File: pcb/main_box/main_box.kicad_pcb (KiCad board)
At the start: 2 copper layers, 150 x 70 mm, 20 parts, among them J1 AudioJack4, J13 Conn_01x06, J2 AudioJack4, J3 AudioJack4, J4 AudioJack4, J5 AudioJack4, J6 AudioJack4, J7 AudioJack4, J8 AudioJack4, SW1 SW_Push, SW2 SW_Push, SW3 SW_Push, SW4 SW_Push, SW5 SW_Push, SW6 SW_Push, U1 Pico

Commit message: Mby somewhat done...
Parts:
- removed J13: Conn_01x06, Connector_JST:JST_XH_B6B-XH-A_1x06_P2.50mm_Vertical
- added J9: Conn_01x06_MountingPin, Audio-jacks Libraries:JST_XH_S6B_combined_1x06, F.Cu at (145.1, 83.8)
- SW1, SW2, SW3, SW4, SW5, SW6: footprint Button_Switch_THT:SW_PUSH_6mm -> Audio-jacks Libraries:SW_PUSH_combined_6mm
- moved H1 16.0 mm to (53.5, 69.5)
- moved H2 16.0 mm to (196.5, 69.5)
- moved J4 5.00 mm to (191.5, 55.2)
- moved J5 5.00 mm to (58.5, 55.2)
- moved J3 4.00 mm to (177.0, 55.2)
- moved J6 4.00 mm to (73.0, 55.2)
- moved J2 3.00 mm to (162.5, 55.2)
- moved J7 3.00 mm to (87.5, 55.2)
- moved SW5 3.00 mm to (140.2, 113.2)
- moved SW6 3.00 mm to (116.2, 113.2)
- moved SW3 2.80 mm to (187.2, 92.0)
- moved SW4 2.80 mm to (178.5, 107.2)
- moved J1 2.00 mm to (148.0, 55.2)
- moved J8 2.00 mm to (102.0, 55.2)
- moved SW1 1.25 mm to (163.2, 98.5)
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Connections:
- J7 pad R2: /GPIO5 -> /GPIO3
- J7 pad T: /GPIO3 -> /GPIO5
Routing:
- net /GPIO5: track 24.4 -> 56.9 mm
- net /GPIO21: track 40.9 -> 64.1 mm
- net /GPIO20: track 56.7 -> 71.8 mm
- net /GPIO19: track 42.3 -> 56.4 mm
- net /GPIO12: track 152.5 -> 165.9 mm
- net /GPIO3: track 40.5 -> 30.5 mm
- net /GPIO13: track 149.2 -> 157.6 mm
- net /GPIO15: track 119.4 -> 127.7 mm
- net /GPIO18: track 51.6 -> 59.8 mm
- net /GPIO16: track 80.4 -> 86.6 mm
- net /GPIO9: track 56.0 -> 62.1 mm
- net /GPIO4: track 43.5 -> 37.4 mm
- net /GPIO17: track 85.5 -> 79.8 mm
- net /GPIO6: track 39.1 -> 44.5 mm
- net /GPIO14: track 140.3 -> 145.1 mm
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
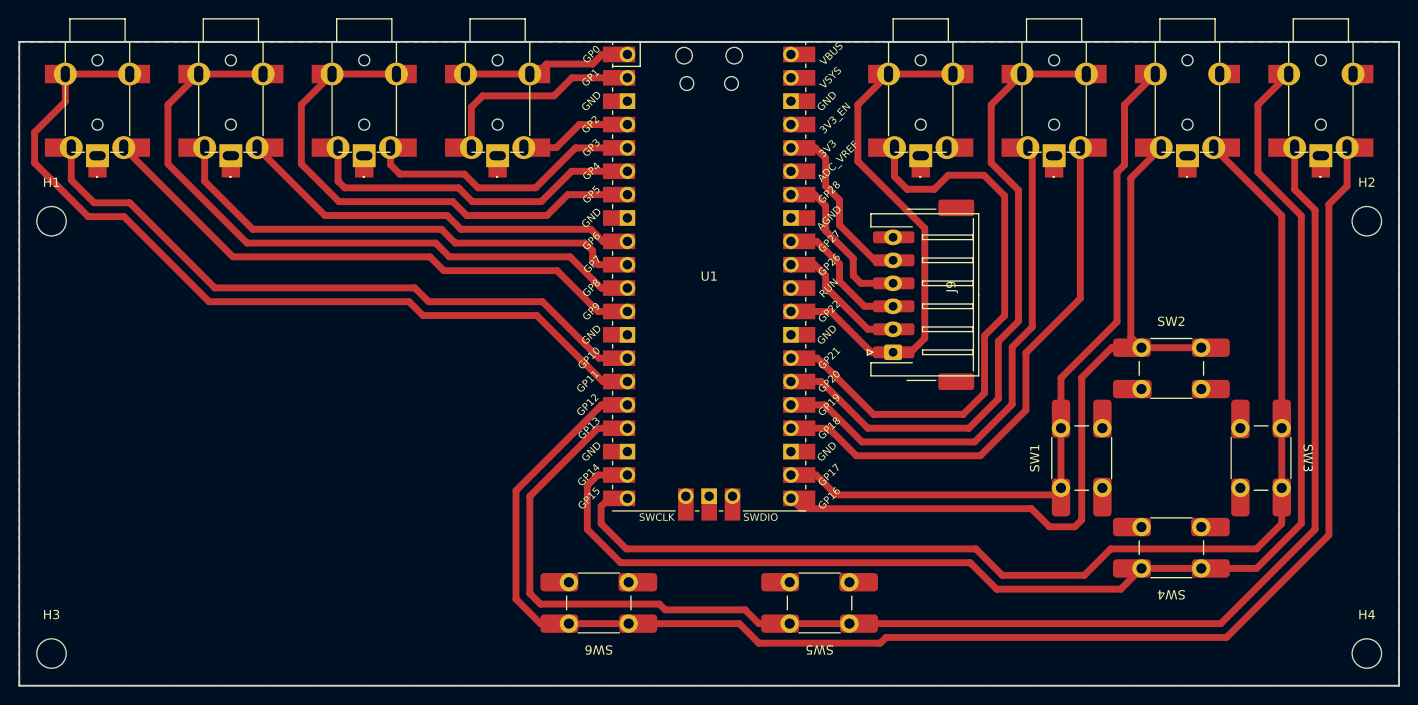
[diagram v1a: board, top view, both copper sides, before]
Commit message: Commiting this in case I do something horribly wrong
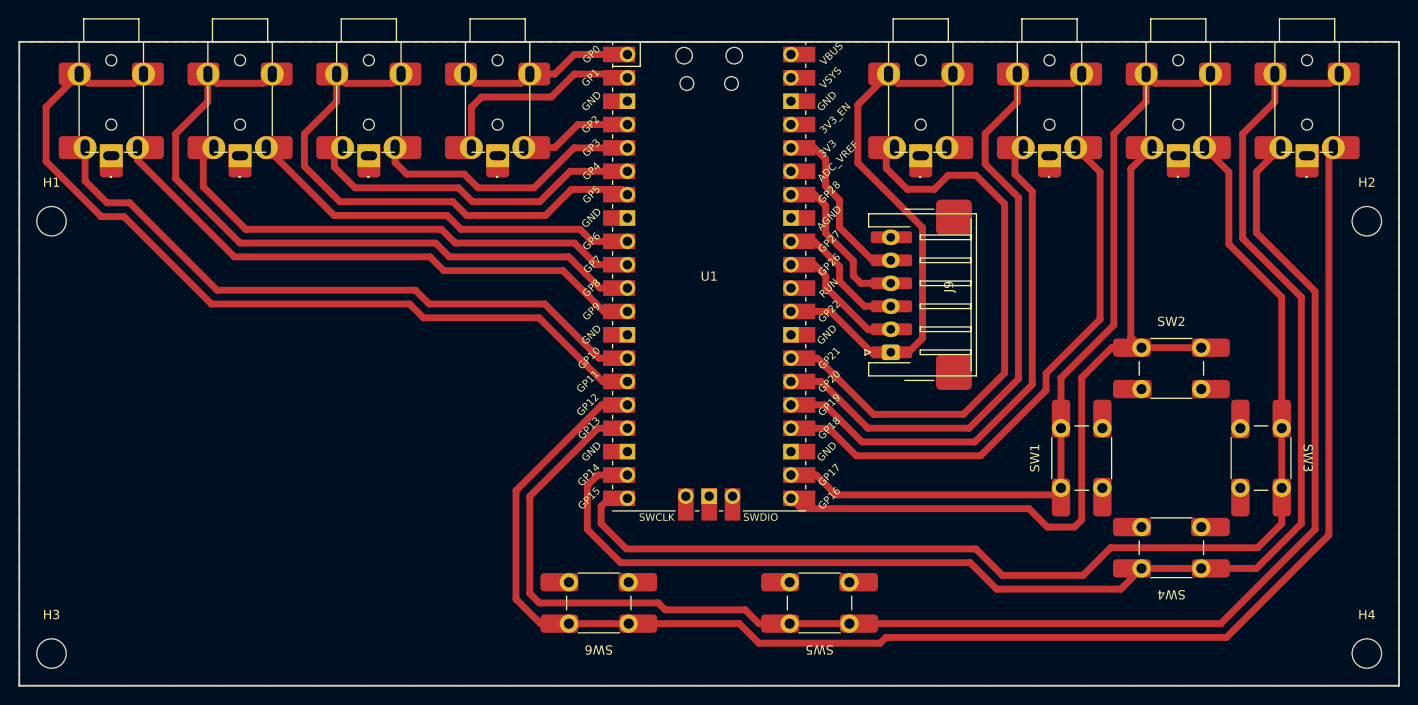
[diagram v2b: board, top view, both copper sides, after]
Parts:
- moved J4 1.50 mm to (190.0, 55.2)
- moved J5 1.50 mm to (60.0, 55.2)
- moved J3 1.00 mm to (176.0, 55.2)
- moved J6 1.00 mm to (74.0, 55.2)
- moved J2 0.50 mm to (162.0, 55.2)
- moved J7 0.50 mm to (88.0, 55.2)
- moved J9 0.25 mm to (144.8, 83.8)
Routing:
- net /GPIO14: track 145.1 -> 153.7 mm
- net /GPIO17: track 79.8 -> 87.2 mm
- net /GPIO13: track 157.6 -> 160.4 mm
- net /GPIO18: track 59.8 -> 61.8 mm
- net /GPIO10: track 72.0 -> 70.6 mm
- net /GPIO20: track 71.8 -> 73.0 mm
- net /GPIO5: track 56.9 -> 58.0 mm
- net /GPIO6: track 44.5 -> 43.5 mm
- net /GPIO8: track 73.7 -> 74.7 mm
- net /GPIO19: track 56.4 -> 57.4 mm
- net /GPIO0: track 17.8 -> 18.6 mm
- net /GPIO9: track 62.1 -> 61.4 mm
- net /GPIO3: track 30.5 -> 29.8 mm
- net /GPIO12: track 165.9 -> 165.3 mm

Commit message: Getting there, just buttons are still small...
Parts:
- added H5: MountingHole, MountingHole:MountingHole_3.2mm_M3, F.Cu at (62.0, 85.0)
- added H6: MountingHole, MountingHole:MountingHole_3.2mm_M3, F.Cu at (88.5, 85.0)
- added H7: MountingHole, MountingHole:MountingHole_3.2mm_M3, F.Cu at (62.0, 105.0)
- added H8: MountingHole, MountingHole:MountingHole_3.2mm_M3, F.Cu at (88.5, 105.0)
- J1, J2, J3, J4, J5, J6, J7, J8: value AudioJack4 -> AudioJack4_SwitchTR1; footprint Audio-jacks Libraries:SJ2_SJ3_combined -> Audio-jacks Libraries:Jack_3.5_PJ31060-I_L_pads
- J9: value Conn_01x06_MountingPin -> Conn_01x05_MountingPin; footprint Audio-jacks Libraries:JST_XH_S6B_combined_1x06 -> Audio-jacks Libraries:JST_XH_S5B_combined_1x05
- moved J4 127.0 mm to (63.0, 57.5), turned to 0 degrees
- moved J5 127.0 mm to (187.0, 57.5), turned to 0 degrees
- moved J3 100.0 mm to (76.0, 57.5), turned to 0 degrees
- moved J6 100.0 mm to (174.0, 57.5), turned to 0 degrees
- moved J2 73.0 mm to (89.0, 57.5), turned to 0 degrees
- moved J7 73.0 mm to (161.0, 57.5), turned to 0 degrees
- moved SW6 63.3 mm to (172.0, 83.2), turned to 0 degrees
- moved SW1 49.3 mm to (116.2, 113.2), turned to 180 degrees
- moved J1 46.1 mm to (102.0, 57.5), turned to 0 degrees
- moved J8 46.1 mm to (148.0, 57.5), turned to 0 degrees
- moved SW2 43.7 mm to (140.2, 113.2), turned to 180 degrees
- moved SW5 27.3 mm to (163.2, 98.5), turned to 90 degrees
- moved SW3 17.6 mm to (178.5, 107.2), turned to 180 degrees
- moved SW4 17.6 mm to (187.2, 92.0), turned to -90 degrees
- moved J9 16.4 mm to (143.5, 67.4), turned to 0 degrees
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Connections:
- J1 pad R1: /GPIO21 -> /GPIO2
- J1 pad R2: unconnected-(J1-PadR2) -> /GPIO0
- J1 pad T: /GPIO22 -> /GPIO1
- J2 pad R1: /GPIO19 -> /GPIO5
- J2 pad R2: /GPIO18 -> /GPIO3
- J2 pad T: /GPIO20 -> /GPIO4
- J3 pad R1: /GPIO16 -> /GPIO8
- J3 pad R2: /GPIO15 -> /GPIO6
- J3 pad T: /GPIO17 -> /GPIO7
- J4 pad R1: /GPIO13 -> /GPIO11
- J4 pad R2: /GPIO12 -> /GPIO9
- J4 pad T: /GPIO14 -> /GPIO10
- J5 pad R1: /GPIO10 -> /GPIO18
- J5 pad R2: /GPIO9 -> /GPIO16
- J5 pad T: /GPIO11 -> /GPIO17
- J6 pad R1: /GPIO7 -> /GPIO21
- J6 pad R2: /GPIO6 -> /GPIO19
- J6 pad T: /GPIO8 -> /GPIO20
- J7 pad R1: /GPIO4 -> /ADC1
- J7 pad R2: /GPIO3 -> +3V3
- J7 pad T: /GPIO5 -> /GPIO22
- J8 pad R1: /GPIO1 -> /ADC2
- J8 pad R2: /GPIO2 -> +3V3
- J8 pad T: /GPIO0 -> /ADC0
- J9 pad 1: /GPIO22 -> /ADC2_N
- J9 pad 2: /ADC0 -> /ADC0_N
- J9 pad 3: /ADC1 -> /GPIO22
- J9 pad 4: /ADC2 -> +3V3
- J9 pad 5: +3V3 -> GND
- SW1 pad 1: /GPIO17 -> /GPIO12
- SW2 pad 1: /GPIO16 -> /GPIO13
- SW3 pad 1: /GPIO15 -> /GPIO14
- SW4 pad 1: /GPIO14 -> /GPIO15
- SW5 pad 1: /GPIO13 -> /GPIO16
- SW6 pad 1: /GPIO12 -> /GPIO17
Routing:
- net /GPIO12: track 165.3 -> 41.1 mm
- net /GPIO13: track 160.4 -> 61.6 mm
- net /GPIO14: track 153.7 -> 69.0 mm
- net +3V3: track 19.4 -> 68.2 mm
- net /ADC1: track 14.7 -> 43.0 mm
- net /GPIO5: track 58.0 -> 38.0 mm
- net /GPIO11: track 91.9 -> 72.4 mm
- net /GPIO8: track 74.7 -> 56.2 mm
- net /GPIO20: track 73.0 -> 55.9 mm
- net /ADC0: track 14.5 -> 28.1 mm
- net /GPIO2: track 12.3 -> 25.7 mm
- net /GPIO15: track 128.1 -> 115.6 mm
- net /GPIO22: track 57.6 -> 45.2 mm
- net /GPIO16: track 86.2 -> 98.3 mm
- net /GPIO7: track 54.4 -> 44.3 mm
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
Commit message: Maybe done, but some refactoring is needed
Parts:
- removed H5, H6, H7, H8: MountingHole, MountingHole:MountingHole_3.2mm_M3
- added H9: Joystick module - 4 MP, Audio-jacks Libraries:Joystick_module_lifted, F.Cu at (61.0, 84.8)
- moved SW5 1.03 mm to (162.2, 98.2)
- moved SW6 1.03 mm to (171.8, 82.2)
- moved SW3 0.56 mm to (178.2, 107.8)
- moved SW4 0.56 mm to (187.8, 91.8)
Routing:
- net /GPIO15: track 115.6 -> 91.8 mm
- net /GPIO17: track 83.2 -> 84.0 mm
- net /GPIO16: track 98.3 -> 99.0 mm
